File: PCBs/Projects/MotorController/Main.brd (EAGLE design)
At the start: 172.7 x 99.1 mm, 112 parts, among them Q1 ZXMP10A17GQ, Q2 MMBT5551LT1G, Q3 BUK9240-100A.118, Q4 BUK9240-100A.118, U1 DRV8301, U11 LT4356-2, U2 ESDA6V1SC6Y, U3 ESDA6V1SC6Y, U4 TMP101, U5 ACS758LCB, U6 ESDA6V1SC6Y, U7 MTI85W100GC, U8 ESDA6V1SC6Y

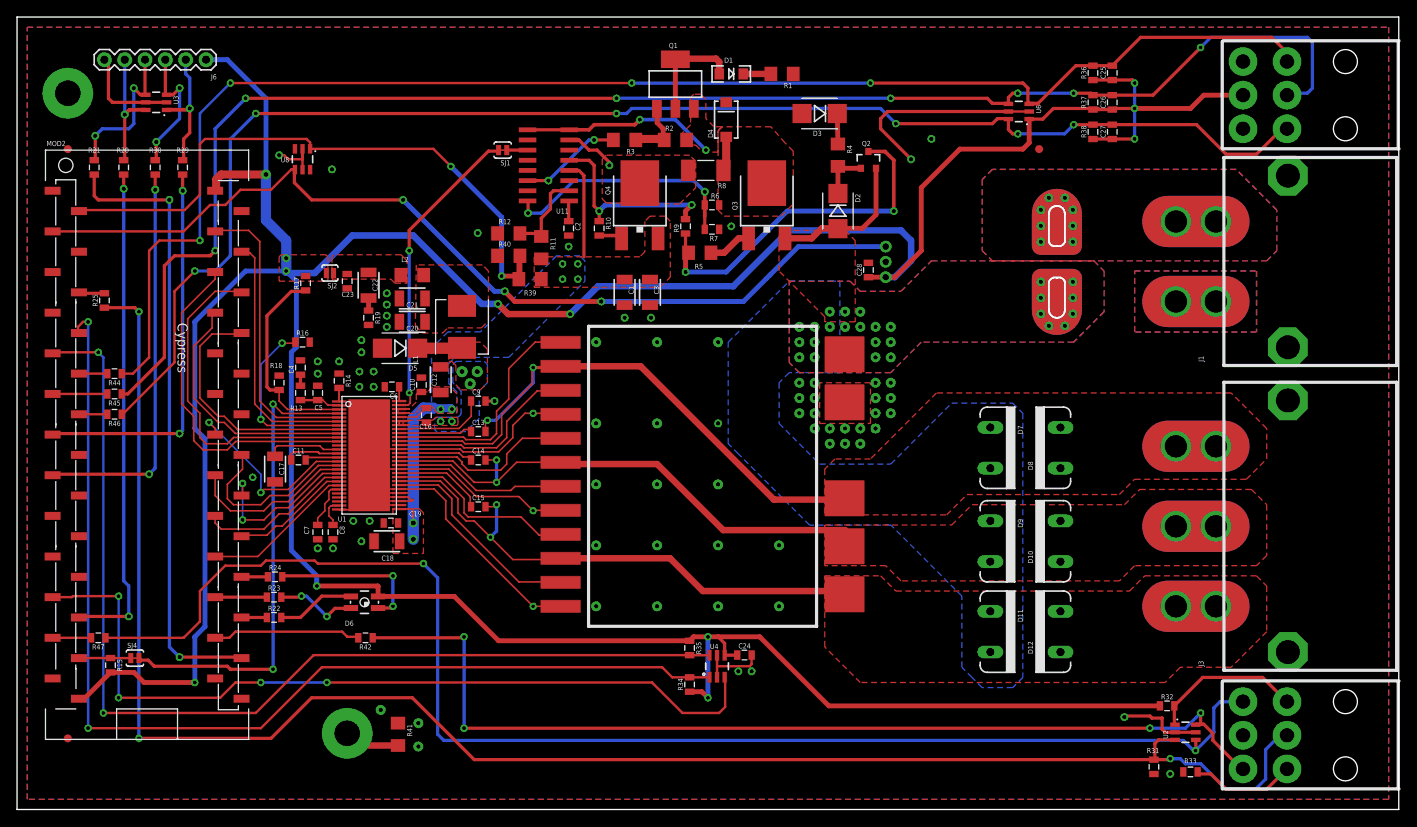
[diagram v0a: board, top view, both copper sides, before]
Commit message: Lots of fine detail work -Mounting holes placed -Silk fixes and additions -SEM added to board
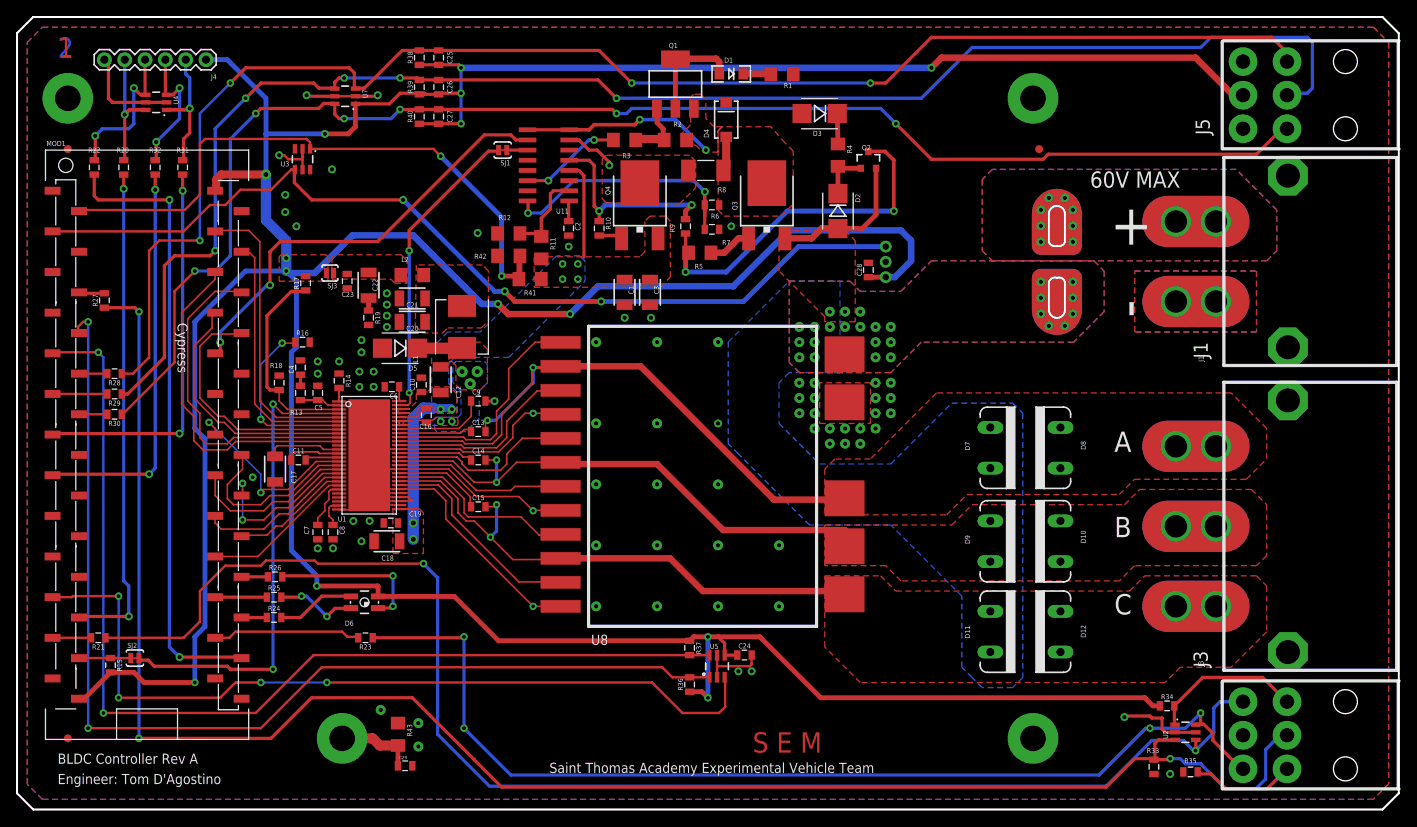
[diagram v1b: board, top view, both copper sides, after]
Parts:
- removed FD4: FIDUCIAL1X2, SparkFun-Aesthetics:FIDUCIAL-1X2
- removed R45, R46, R47: 100, SparkFun-Resistors:0805
- removed S6: STANDOFF_ELECTRICAL, SparkFun-Electromechanical:STANDOFF-ELECTRICAL
- removed SJ4: SOLDERJUMPERTRACE, SparkFun-Retired:SJ_2S-TRACE
- added C29: 0.01u, SparkFun-Capacitors:0805
- added FD1: FIDUCIAL1X2, SparkFun-Aesthetics:FIDUCIAL-1X2
- added R26: 330, SparkFun-Resistors:0805
- added R27: 100, SparkFun-Resistors:0805
- added R43: 1M, SparkFun-Resistors:1206
- added S2, S3, S4: STANDOFF_ELECTRICAL, SparkFun-Electromechanical:STANDOFF-ELECTRICAL
- added SJ3: SOLDERJUMPERNO, SparkFun-Retired:SJ_2S-NO
- R22, R23: value 330 -> 100
- R25: value 100 -> 330
- R31: value 510k -> 100
- R32: value 1k -> 100
- R33: value 1k -> 510k
- R34, R35: value 4.7k -> 1k
- R36, R37: value 10k -> 4.7k
- R39: value 100k -> 10k; device SparkFun-Resistors:1206 -> SparkFun-Resistors:0805
- R40: value 5.1k -> 10k; device SparkFun-Resistors:1206 -> SparkFun-Resistors:0805
- R41: value 1M -> 100k
- R42: value 100 -> 5.1k; device SparkFun-Resistors:0805 -> SparkFun-Resistors:1206
- SJ2: value SOLDERJUMPERNO -> SOLDERJUMPERTRACE; device SparkFun-Retired:SJ_2S-NO -> SparkFun-Retired:SJ_2S-TRACE
- U4: value TMP101 -> ESDA6V1SC6Y; device SparkFun-DigitalIC:SOT23-6 -> IC:SOT23-6
- U5: value ACS758LCB -> TMP101; device IC:CB5PIN -> SparkFun-DigitalIC:SOT23-6
- U6: value ESDA6V1SC6Y -> ACS758LCB; device IC:SOT23-6 -> IC:CB5PIN
- U7: value MTI85W100GC -> ESDA6V1SC6Y; device IC:ISOPLUS-DIL -> IC:SOT23-6
- U8: value ESDA6V1SC6Y -> MTI85W100GC; device IC:SOT23-6 -> IC:ISOPLUS-DIL
- moved R32 143.3 mm to (17.3, 77.7), turned to 270 degrees
- moved R31 142.7 mm to (20.7, 77.7)
- moved FD2 121.4 mm to (6.35, 80.0)
- moved U4 99.4 mm to (17.4, 85.9), turned to 270 degrees
- moved R36 91.6 mm to (84.1, 13.1)
- moved R37 84.8 mm to (84.1, 17.7), turned to 270 degrees
- moved R38 84.7 mm to (50.3, 91.4)
- moved C25 84.2 mm to (52.7, 91.4)
- moved C26 84.2 mm to (52.7, 87.8)
- moved C27 84.2 mm to (52.7, 84.1)
- moved U7 69.2 mm to (41.0, 86.6), turned to 270 degrees
- moved U8 64.5 mm to (67.9, 22.9)
- moved R35 64.5 mm to (146.7, 2.16), turned to 180 degrees
- moved R22 60.6 mm to (9.65, 77.7), turned to 270 degrees
- moved R34 59.7 mm to (143.8, 10.4), turned to 0 degrees
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- renumbered FD6 to FD3, J6 to J4, MOD2 to MOD1, R44 to R28
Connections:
- net !IN-FAULT: now also MOD1.44
- net 5V: now also R39.1, R40.1, SJ3.2, U5.4, U7.1; no longer R32.1, R35.1, SJ2.2, U4.4, U5.1
- net A: now also U8.L1, U8.S1; no longer U7.L1, U7.S1
- net B: now also U8.L2, U8.S3; no longer U7.L2, U7.S3
- net C: now also U8.L3, U8.S5; no longer U7.L3, U7.S5
- net DISABLE: now also R23.1; no longer R42.1
- net DISP_OUT: now also R22.1, U4.4; no longer R21.1, U3.4
- net GH_A: now also U8.G1; no longer U7.G1
- net GH_B: now also U8.G3; no longer U7.G3
- net GH_C: now also U8.G5; no longer U7.G5
- net GL_A: now also U8.G2; no longer U7.G2
- net GL_B: now also U8.G4; no longer U7.G4
- net GL_C: now also U8.G6; no longer U7.G6
- net GND: now also C29.2, R35.2, R42.1, R43.1, U5.5, U7.2, U7.5, U8.L-, U8.S2, U8.S4, U8.S6; no longer R31.2, R40.1, R41.1, U6.5, U7.L-, U7.S2, U7.S4, U7.S6, U8.2, U8.5
- net GPIO_TBD: now also U4.6; no longer U3.6
- net H1: now also R38.2, U7.3; no longer R36.2, U6.3
- net H2: now also R29.1, R39.2, U7.4; no longer R37.2, R45.1, U6.4
- net H3: now also R30.1, R40.2, U7.6; no longer R38.2, R46.1, U6.6
- net ISENSE: now also U3.4, U6.3; no longer U5.3, U8.4
- net MONITOR_RX: now also R32.1, U4.3; no longer R30.1, U3.3
- net MONITOR_TX: now also R31.1, U4.1; no longer R29.1, U3.1
- net N$16: now also R23.2; no longer R42.2
- net N$31: now also C29.1, R43.2; no longer R41.2
- net N$32: now also R26.1; no longer R24.1
- net N$33: now also R25.1; no longer R23.1
- net N$34: now also R24.1; no longer R22.1
- net N$35: now also R26.2; no longer R24.2
- net N$36: now also R25.2; no longer R23.2
- net N$37: now also R24.2; no longer R22.2
- net N$39: now also R27.2; no longer R25.2
- net N$41: now also R22.2; no longer R21.2
- net N$43: now also R31.2; no longer R29.2
- net N$44: now also R32.2; no longer R30.2
- net N$45: now also SJ2.2; no longer SJ4.2
- net N$47: now also R29.2; no longer R45.2
- net N$48: now also R30.2; no longer R46.2
- net N$49: now also R21.2; no longer R47.2
- net PREJUMP_5V: now also SJ3.1; no longer SJ2.1
- net PWRGD: now also SJ2.1; no longer SJ4.1
- net REVERSE: now also R21.1; no longer R47.1
- net SCL: now also R36.2, U5.1; no longer R34.2, U4.1
- net SDA: now also R37.2, U5.6; no longer R35.2, U4.6
- net THROTTLE_1: now also R34.2; no longer R32.2
- net THROTTLE_2: now also R27.1, R33.1; no longer R25.1, R31.1
- net THROTTLE_3: now also R35.1; no longer R33.1
- net T_ALERT: now also U5.3; no longer U4.3
- net VCC: now also R41.2; no longer R39.2
- net VIN: now also U6.4_1, U6.4_2, U6.4_3, U6.4_4, U6.4_5, U6.4_6, U6.4_7, U6.4_8; no longer U5.4_1, U5.4_2, U5.4_3, U5.4_4, U5.4_5, U5.4_6, U5.4_7, U5.4_8
- net VSENSE: now also R41.1, R42.2, U3.1; no longer R39.1, R40.2, U8.1
- net V_BATT: now also U6.5_1, U6.5_2, U6.5_3, U6.5_4, U6.5_5, U6.5_6, U6.5_7, U6.5_8, U8.L+; no longer U5.5_1, U5.5_2, U5.5_3, U5.5_4, U5.5_5, U5.5_6, U5.5_7, U5.5_8, U7.L+
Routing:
- net 5V: track 464.0 -> 531.9 mm, vias 12 -> 14
- net !IN-FAULT: track 0.00 -> 54.6 mm, vias 0 -> 2
- net GND: track 189.1 -> 173.0 mm, vias 72 -> 79
- net DISABLE: track 126.5 -> 131.3 mm
- net REVERSE: track 175.4 -> 180.1 mm
- net H1: track 186.5 -> 189.8 mm
- net THROTTLE_2: track 218.0 -> 221.0 mm
- net N$31: track 6.98 -> 9.89 mm
- net H2: track 193.7 -> 195.6 mm, vias 7 -> 5
- net H3: track 181.3 -> 182.4 mm
- net A: track 80.0 -> 80.7 mm
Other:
- outline, holes or cut-outs redrawn
- board text added: "+"
- board text added: "-"
- board text added: "1"
- board text added: "2"
- board text added: "60V MAX"
- board text added: "A"
- board text added: "B"
- board text added: "BLDC Controller Rev A"
- board text added: "C"
- board text added: "Engineer: Tom D'Agostino"
- board text added: "J1"
- board text added: "J3"
- board text added: "J5"
- board text added: "S E M"
- board text added: "Saint Thomas Academy Experimental Vehicle Team"

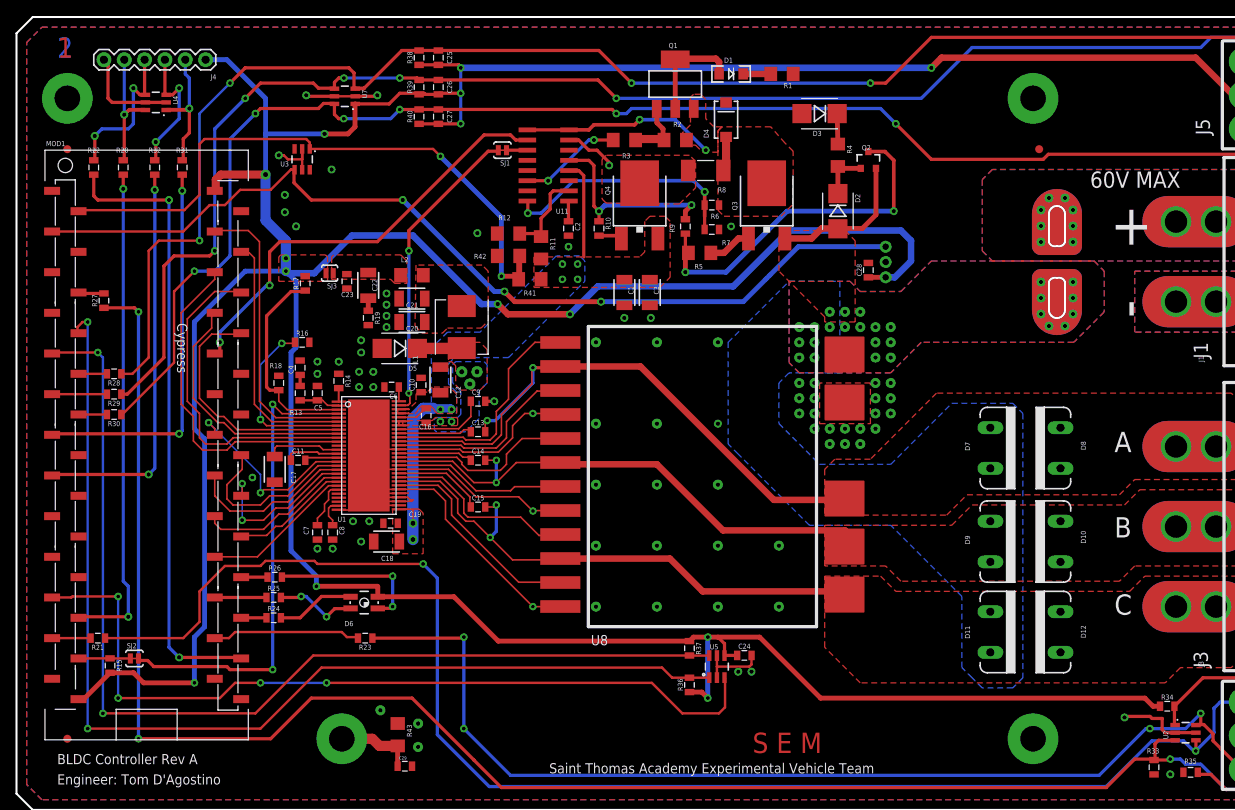
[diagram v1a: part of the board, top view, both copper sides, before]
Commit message: Laundry list of fixes -Changed feedback point for buck convert -Labeled layers in copper -Added filter cap to current sense line -Fixed footprint of acs758
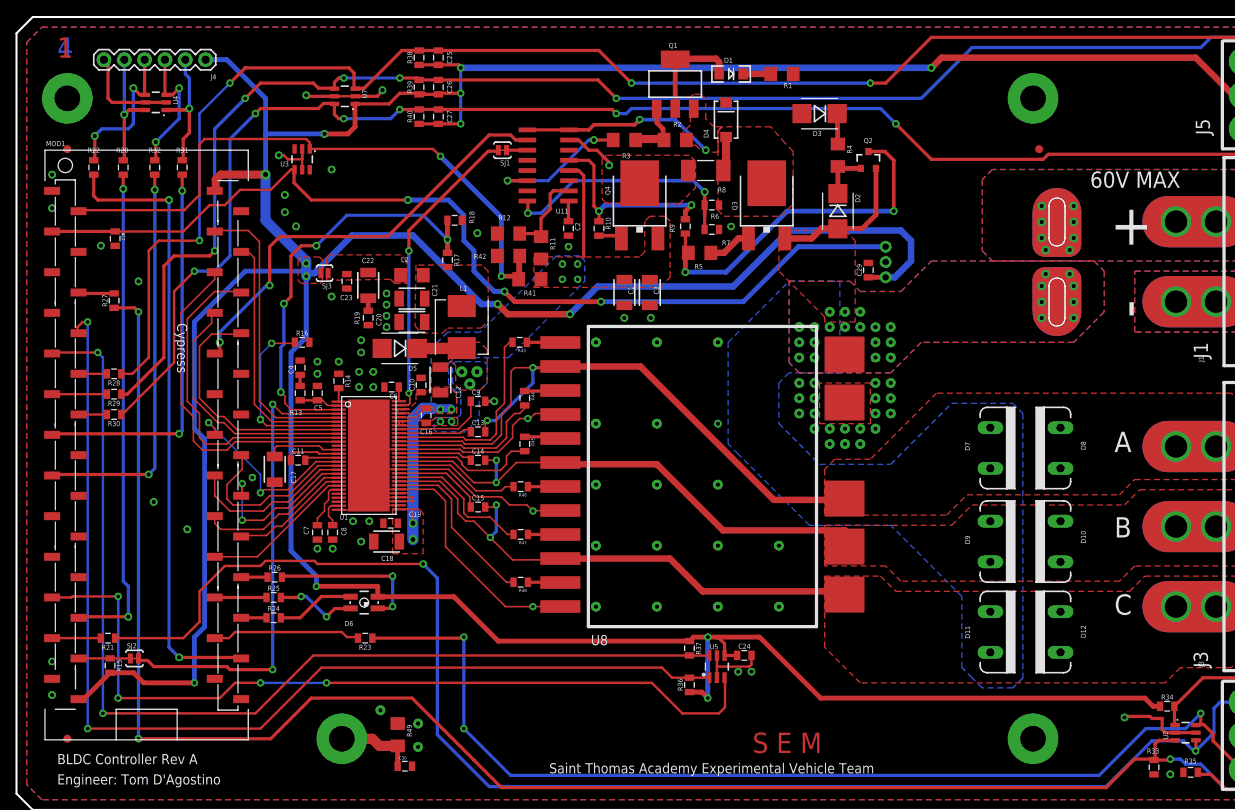
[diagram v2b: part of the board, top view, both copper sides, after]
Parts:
- added C30: 0.01u, SparkFun-Capacitors:0805
- added R44, R45, R46, R47, R48: 10, SparkFun-Resistors:0805
- added R49: 1M, SparkFun-Resistors:1206
- C28: value 0.1u -> 10n
- C29: value 0.01u -> 0.1u
- R43: value 1M -> 10; device SparkFun-Resistors:1206 -> SparkFun-Resistors:0805
- moved C28 94.2 mm to (12.3, 68.8), turned to 270 degrees
- moved C29 84.8 mm to (106.4, 64.9), turned to 90 degrees
- moved R43 51.3 mm to (62.9, 55.9), turned to 180 degrees
- moved R18 29.9 mm to (54.7, 71.1), turned to 180 degrees
- moved R17 18.0 mm to (53.8, 66.2), turned to 270 degrees
- moved R21 1.27 mm to (11.4, 18.9)
- moved R27 1.27 mm to (12.2, 61.1)
- moved SJ3 0.63 mm to (38.5, 64.5)
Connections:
- new net N$27: R45.1, U8.G3
- new net N$28: R43.1, U8.G1
- new net N$38: R44.1, U8.G2
- new net N$50: R46.1, U8.G4
- new net N$51: R47.1, U8.G5
- new net N$52: R48.1, U8.G6
- net 5V: now also C29.1; no longer C28.1, R17.2
- net GH_A: now also R43.2; no longer U8.G1
- net GH_B: now also R45.2; no longer U8.G3
- net GH_C: now also R47.2; no longer U8.G5
- net GL_A: now also R44.2; no longer U8.G2
- net GL_B: now also R46.2; no longer U8.G4
- net GL_C: now also R48.2; no longer U8.G6
- net GND: now also C30.2, R49.1; no longer R43.1
- net IND_LOOP_OUT: now also R17.2
- net ISENSE: now also C28.1
- net N$31: now also C30.1, R49.2; no longer C29.1, R43.2
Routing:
- net N$14: track 26.0 -> 53.2 mm, vias 0 -> 4
- net GL_B: track 24.0 -> 15.8 mm
- net GH_C: track 25.4 -> 18.3 mm
- net GH_B: track 23.5 -> 18.1 mm
- net GL_A: track 24.7 -> 19.5 mm
- net GL_C: track 26.4 -> 21.4 mm
- net UNDERVOLTAGE: track 12.8 -> 17.8 mm
- net GH_A: track 29.9 -> 25.1 mm
- net N$27: track 0.00 -> 4.54 mm
- net N$38: track 0.00 -> 4.47 mm
- net N$28: track 0.00 -> 4.19 mm
- net N$52: track 0.00 -> 4.07 mm
- net N$51: track 0.00 -> 4.06 mm
- net N$50: track 0.00 -> 4.06 mm
- net ISENSE: track 118.1 -> 122.1 mm
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- added copper zone on layer 2, net A
- added copper zone on layer 2, net B
- added copper zone on layer 2, net C
- added copper zone on layer 15, net GND
- added copper zone on layer 2, net GND
- added copper zone on layer 15, net IND_LOOP_IN
- added copper zone on layer 2, net VIN
- added copper zone on layer 2, net V_BATT
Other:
- board text added: "3"
- board text added: "4"
